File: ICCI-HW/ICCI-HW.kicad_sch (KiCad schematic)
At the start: 0 parts

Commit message: usb PD started
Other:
- sheet BATT renamed BATT + POWER
- sheet PS + USB renamed USB
- sheet BATT + POWER: file BATT.kicad_sch -> BATT+POWER.kicad_sch
- sheet USB: file PS_USB.kicad_sch -> USB.kicad_sch

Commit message: updated
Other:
- note added: "# TODO - Batteria con comparatore per low voltage (unmount sd card etc..) - Testpoints - MH - Controllare PIN - controllare led"
- note removed: "# TODO - Batteria con comparatore per low voltage (unmount sd card etc..) - Circuito ricarica batteria - Testpoints - MH - Controllare PIN - controllare led - IR"

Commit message: updated
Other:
- sheet AUX + Peripherals ports: added Buzzer, GPS_EXTINT, GPS_TP, LED_B, LED_G, LED_R, SCL1, SDA1, SD_S_LED, VSPI_CLK, VSPI_MISO, VSPI_MOSI, ~{GPS_RESET}, ~{SAFEBOOT}, ~{SD_CS}; removed none
- sheet BATT + POWER ports: added 1V8_EN, 1V8_PG, CHR0, CHR1, CHREN, SCL1, SDA1, VBUS; removed none
- sheet ESP ports: added Buzzer, DS_DQ, EN, IO0, LED_B, LED_G, LED_R, LOG_EN, RXD, SCL0, SCL1, SDA0, SDA1, SD_S_LED, TXD, VBUS, VSPI_CLK, VSPI_MISO, VSPI_MOSI, ~{SD_CS}; removed none
- sheet Sensors ports: added DS_DQ, SCL0, SDA0; removed none
- sheet USB ports: added CHR0, CHR1, CHREN, EN, IO0, RXD, TXD, VBUS; removed none
- note added: "Completed: Check:"
- note added: "Completed: OK Check:"

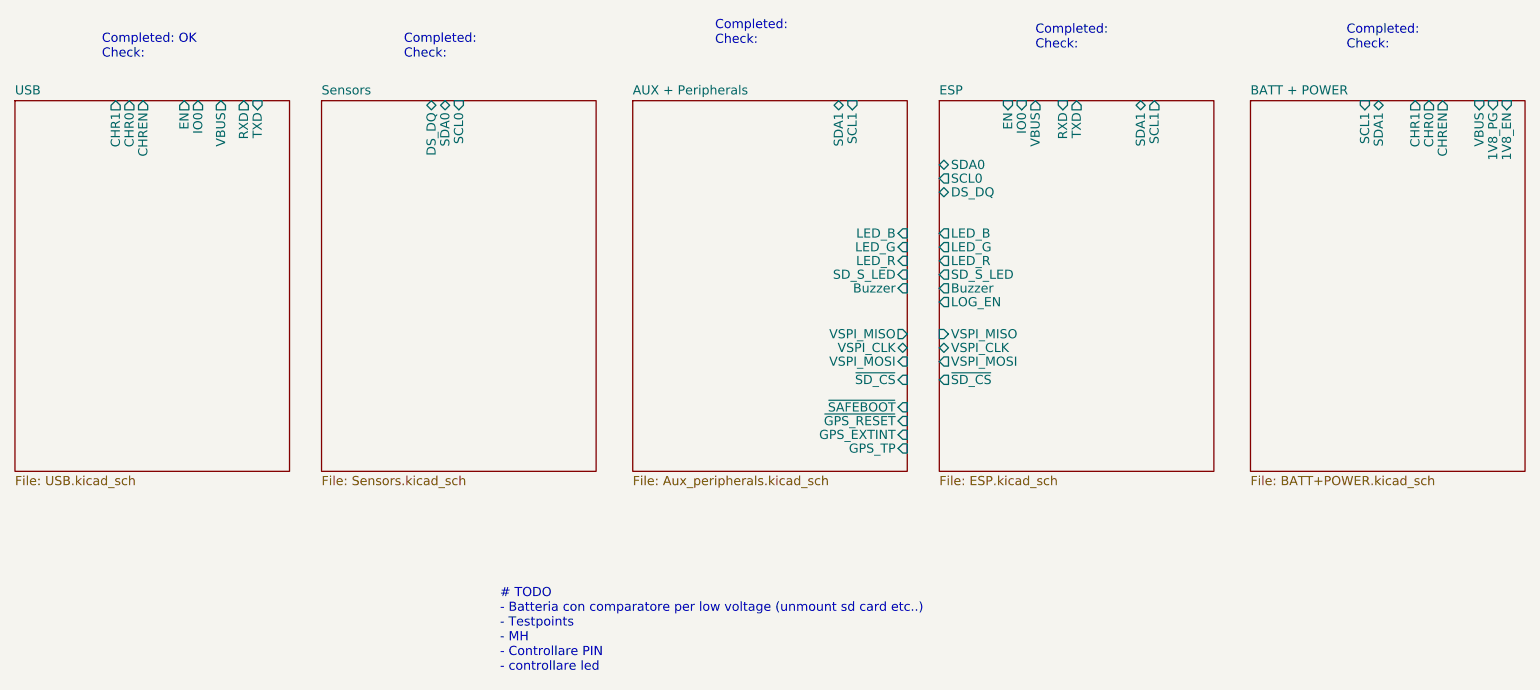
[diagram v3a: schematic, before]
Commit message: add GPIO Expansion
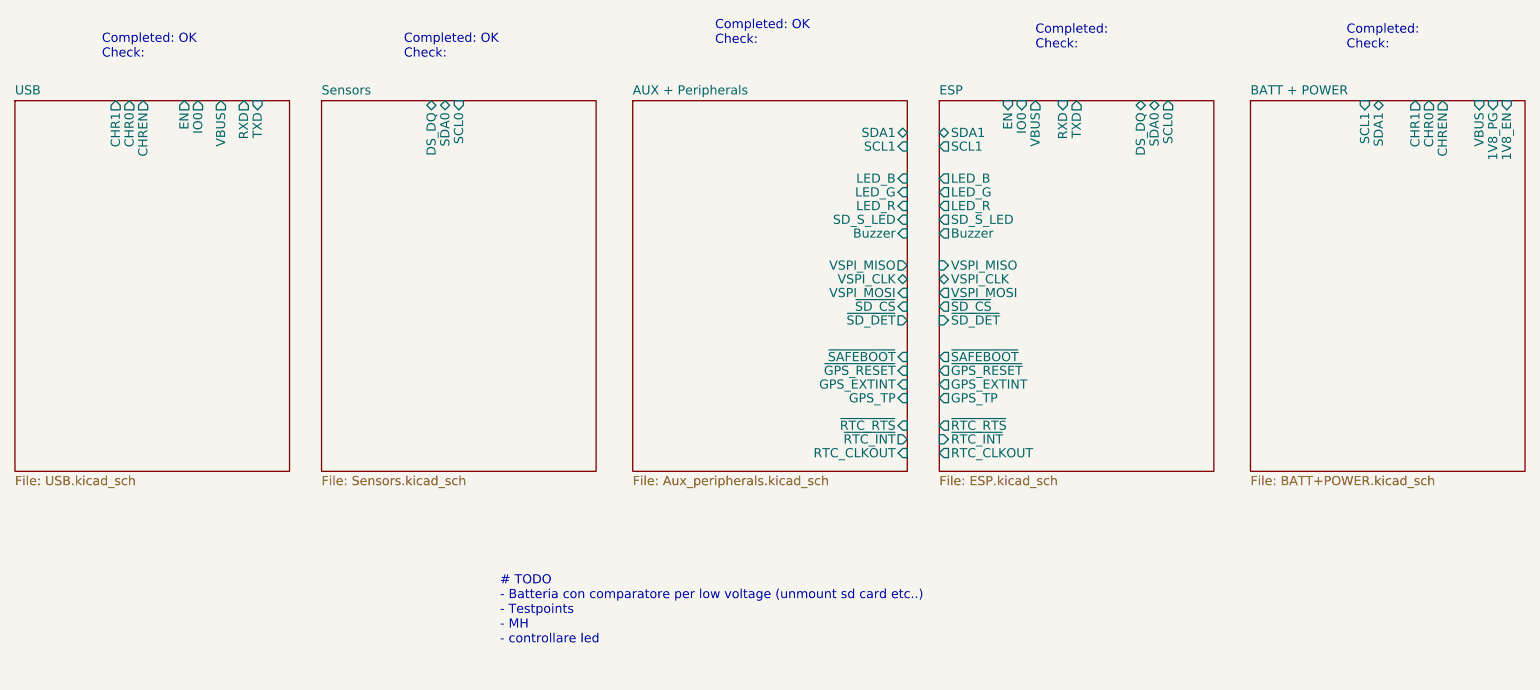
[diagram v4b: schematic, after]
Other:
- sheet AUX + Peripherals ports: added RTC_CLKOUT, ~{RTC_INT}, ~{RTC_RTS}, ~{SD_DET}; removed none
- sheet ESP ports: added GPS_EXTINT, GPS_TP, RTC_CLKOUT, ~{GPS_RESET}, ~{RTC_INT}, ~{RTC_RTS}, ~{SAFEBOOT}, ~{SD_DET}; removed LOG_EN
- note added: "# TODO - Batteria con comparatore per low voltage (unmount sd card etc..) - Testpoints - MH - controllare led"
- note removed: "# TODO - Batteria con comparatore per low voltage (unmount sd card etc..) - Testpoints - MH - Controllare PIN - controllare led"
